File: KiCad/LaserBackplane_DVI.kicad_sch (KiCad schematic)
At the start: 45 parts, among them J1 Curr. Mod., J2 DVI-I, J3 Ld+, J4 Ld-, J5 Pz+, J6 Pz-, J7 Piezo_In, K1 G6AU, Q1 MMBT3904, Q2 2N4401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

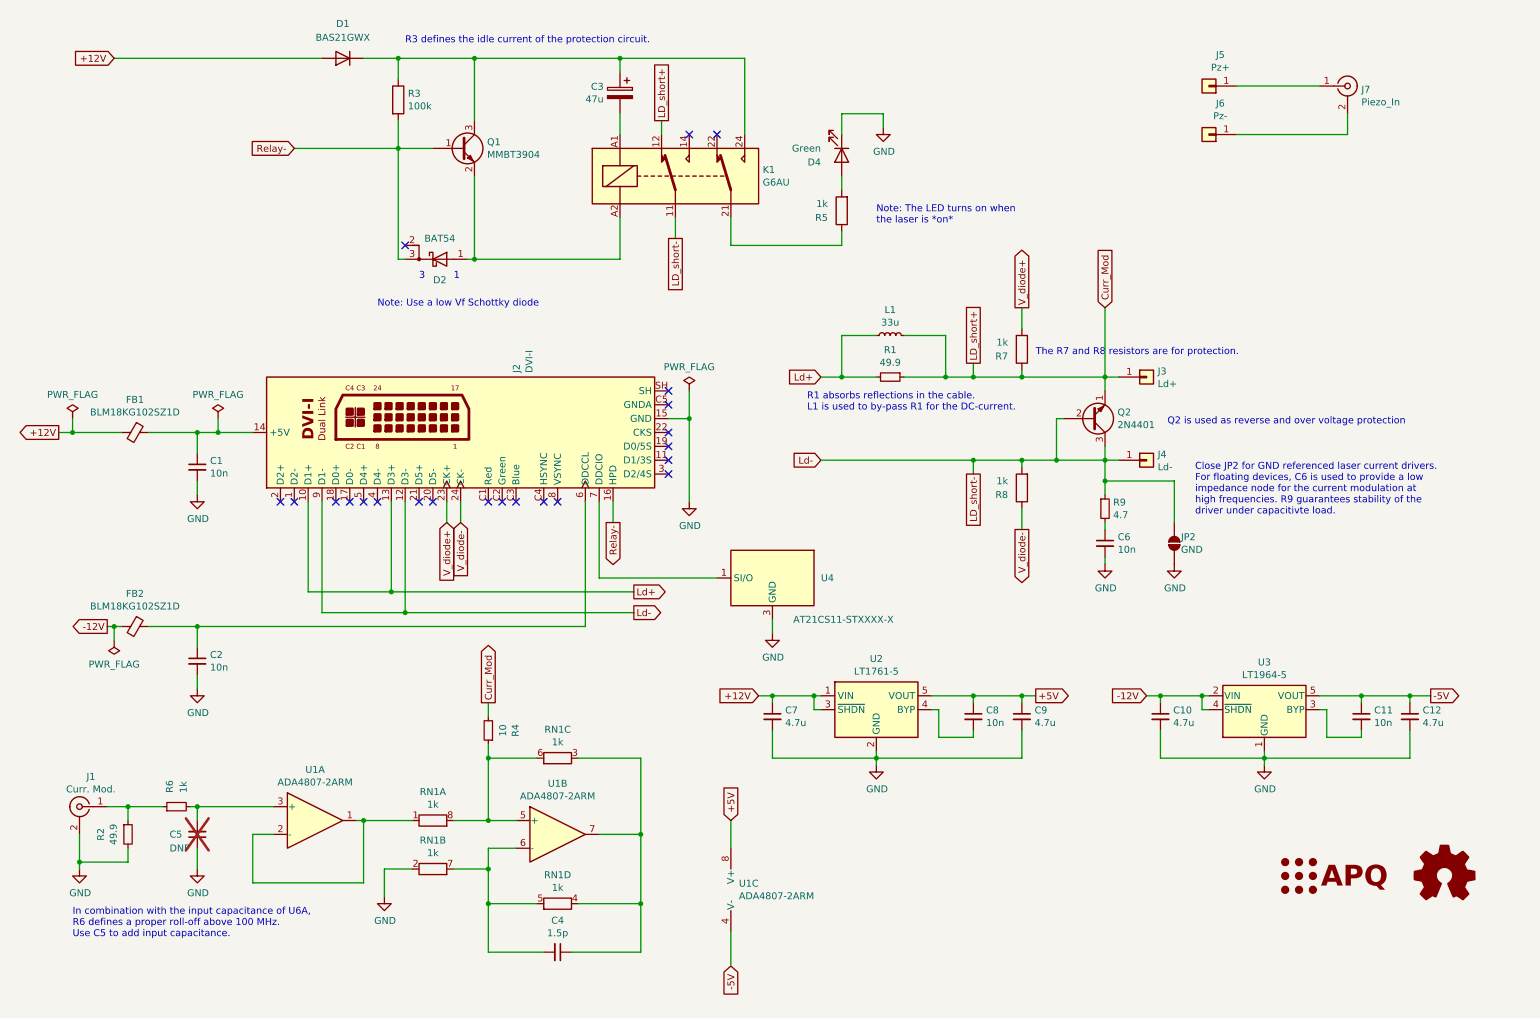
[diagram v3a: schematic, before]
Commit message: Updated parts
- Swapped 50 ohm resistor for a higher wattage part
- Added bypass capacitors to the current source opamp
- Put all parts on a 0.25 mm grid
- Improved routing
- Removed ground layer keepout below the current source, because there is no significant coupling at 1.6 mm distance
- Added RoHS information
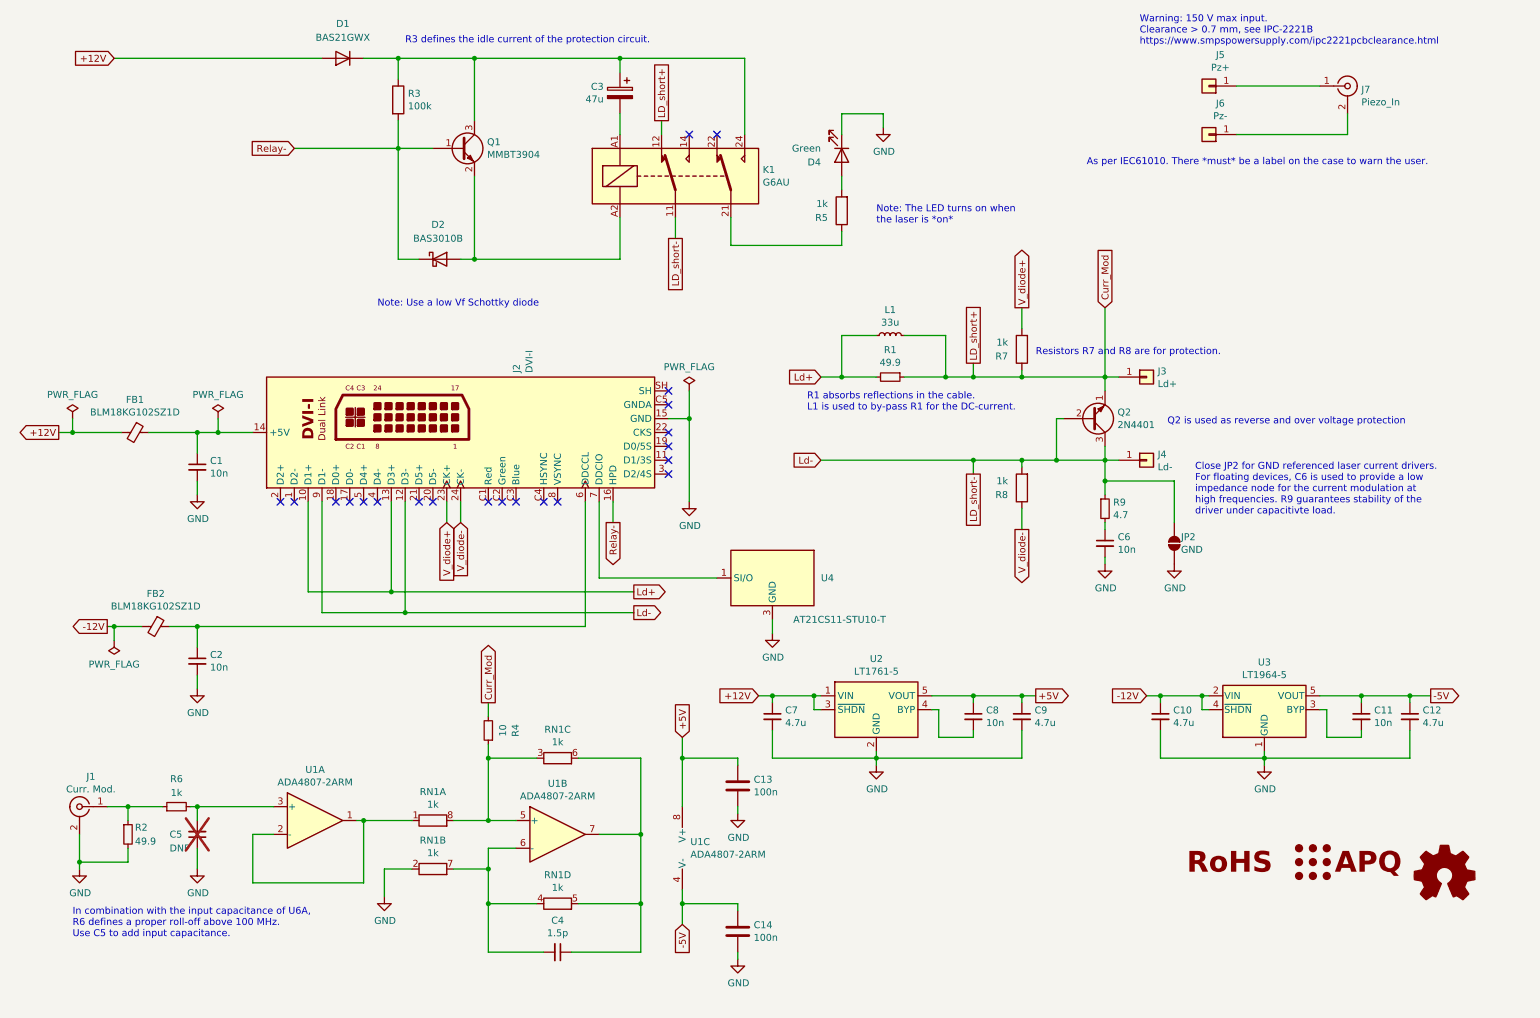
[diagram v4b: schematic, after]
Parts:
- removed D2: BAT54, Package_TO_SOT_SMD:SOT-23, symbol Device:D_Schottky_AKK
- added C13, C14: 100n, Capacitor_SMD:C_0603_1608Metric, symbol Device:C
- added D2: BAS3010B, Diode_SMD:D_SOD-323, symbol Device:D_Schottky
- added LOGO3: Logo_RoHS, Symbol:RoHS-Logo_6mm_SilkScreen, symbol Custom_logos:SYM_RoHS
- C1, C11, C2, C6, C8, FB1, FB2, RN1: RoHS (none) -> Yes; Temperature (none) -> Tstorage = –55 °C to 125 °C
- C10, C12, C7, C9: MFN Murata Electronics -> TDK; PN GRM21BR61H475KE51L -> CGA4J1X7R1V475K125AC; RoHS (none) -> Yes; Temperature (none) -> Tstorage = –55 °C to 125 °C
- C3: RoHS (none) -> Yes; Temperature (none) -> Tstorage = –40 °C to 105 °C
- C4: MFN Yageo -> Kemet; PN CC0603CPNPO9BN1R5 -> C0603C159C5GACAUTO; RoHS (none) -> Yes; Temperature (none) -> Tstorage = –55 °C to 125 °C
- D1: RoHS (none) -> Yes; Temperature (none) -> Tstorage = –65 °C to 150 °C
- D4: RoHS (none) -> Yes; Temperature (none) -> Tstorage = –40 °C to 85 °C
- J1: RoHS (none) -> By exemption; Temperature (none) -> Tstorage = –65 °C to 165 °C
- J2: MFN Conn_Link -> Conn-Link Technology Inc.; RoHS (none) -> Yes; Temperature (none) -> Tstorage = –20 °C to 85 °C
- J7: RoHS (none) -> Yes; Temperature (none) -> Tstorage = –65 °C to 165 °C
- K1: RoHS (none) -> Yes; Temperature (none) -> Tstorage = –40 °C to 70 °C
- L1: RoHS (none) -> Yes; Temperature (none) -> Tstorage = –40 °C to 165 °C
- Q1: PN MMBT3904VL -> MMBT3904-QR; RoHS (none) -> Yes; Temperature (none) -> Tstorage = –65 °C to 150 °C
- Q2: RoHS (none) -> Yes; Temperature (none) -> Tstorage = –55 °C to 150 °C
- R1: footprint Resistor_SMD:R_0603_1608Metric -> Resistor_SMD:R_0805_2012Metric; PN RR0816Q-49R9-D-68R -> RG2012P-49R9-D-T5; RoHS (none) -> Yes; Temperature (none) -> Tstorage = –55 °C to 155 °C
- R2: footprint Resistor_SMD:R_1210_3225Metric -> Resistor_SMD:R_0612_1632Metric; MFN Yageo -> ROHM Semiconductor; PN RC1210FR-0749R9L -> LTR18EZPF49R9; RoHS (none) -> By exemption; Temperature (none) -> Tstorage = –55 °C to 155 °C
- R3: RoHS (none) -> By exemption; Temperature (none) -> Tstorage = –55 °C to 155 °C
- R4: PN RR0816Q-100-D -> RG1608Q-100-D-T5; RoHS (none) -> Yes; Temperature (none) -> Tstorage = –55 °C to 155 °C
- R5, R6, R7, R8: RoHS (none) -> Yes; Temperature (none) -> Tstorage = –55 °C to 155 °C
- R9: MFN Panasonic -> SEI Stackpole; PN ERJ-3RQF4R7V -> RNCP0603FTD4R70; RoHS (none) -> Yes; Temperature (none) -> Tstorage = –55 °C to 155 °C
- U1: RoHS (none) -> Yes; Temperature (none) -> Tstorage = –40 °C to 125 °C
- U2: PN LT1761ES5-5#TRPBF -> LT1761IS5-5#TRPBF; RoHS (none) -> Yes; Temperature (none) -> Tstorage = –40 °C to 125 °C
- U3: PN LT1964ES5-5#TRPBF -> LT1964IS5-5#TRPBF; RoHS (none) -> Yes; Temperature (none) -> Tstorage = –40 °C to 125 °C
- U4: value AT21CS11-STXXXX-X -> AT21CS11-STU10-T; MFN (none) -> Microchip Technology; PN (none) -> AT21CS11-STU10-T; RoHS (none) -> Yes; Temperature (none) -> Tstorage = –40 °C to 85 °C
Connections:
- net +5V: now also C13.1
- net -5V: now also C14.1
- net GND: now also C13.2, C14.2
- net Relay-: now also D2.1 (K)
- net at K1.A2, Q1.2 (E): now also D2.2 (A)
- net at R4.1, RN1.8 (R1.2), U1.5 (+): now also RN1.3 (R3.1); no longer RN1.6 (R3.2)
- net at C4.2, RN1.7 (R2.2), U1.6 (-): now also RN1.4 (R4.1); no longer RN1.5 (R4.2)
- net at C4.1, U1.7: now also RN1.5 (R4.2), RN1.6 (R3.2); no longer RN1.3 (R3.1), RN1.4 (R4.1)
- no-connect marks 22 -> 21
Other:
- note added: "As per IEC61010. There *must* be a label on the case to warn the user."
- note added: "Resistors R7 and R8 are for protection."
- note added: "Warning: 150 V max input. Clearance > 0.7 mm, see IPC-2221B https://www.smpspowersupply.com/ipc2221pcbclearance.html"
- note removed: "1"
- note removed: "3"
- note removed: "The R7 and R8 resistors are for protection."
- moved on the sheet: FB2, RN1C, RN1D, U1C

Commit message: Place bypass capacitors only when using the current mod variant
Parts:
- C13, C14: Config (none) -> +curr_mod; variant (none) -> curr_mod
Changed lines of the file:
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@@
+			)
+		)
+		(property "Config" "+curr_mod"
+			(at 146.05 184.15 0)
+			(effects
+				(font
+					(size 1.27 1.27)
+				)
+				(hide yes)
+			)
+		)
+		(property "variant" "curr_mod"
+			(at 146.05 184.15 0)
+			(effects
+				(font
+					(size 1.27 1.27)
+				)
+				(hide yes)
 			)
 		)
@@
 				)
 				(hide yes)
+			)
+		)
+		(property "Config" "+curr_mod"
+			(at 146.05 157.48 0)
+			(effects
+				(font
+					(size 1.27 1.27)
+				)
+				(hide yes)
+			)
+		)
+		(property "variant" "curr_mod"
+			(at 146.05 157.48 0)
+			(effects
+				(font
+					(size 1.27 1.27)
+				)
+				(hide yes)

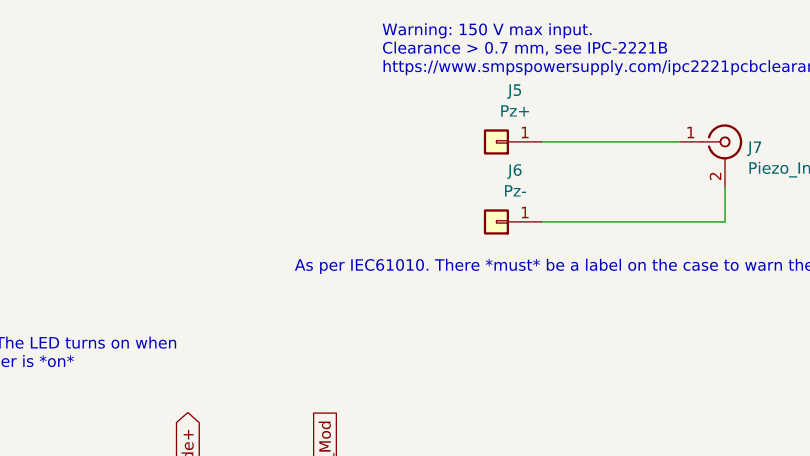
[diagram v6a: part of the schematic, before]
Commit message: 1.7.4 (#5)
* Add chamfer to corners

* Change line with of the part dimentsions to 0.1 mm

* Add teardrops

* Added peizo driver high voltage warning

* Add PCBA variant

* Cleaned up labels

* Create individual gerber files for all variants to make sure DNP parts are not included in the mask layer
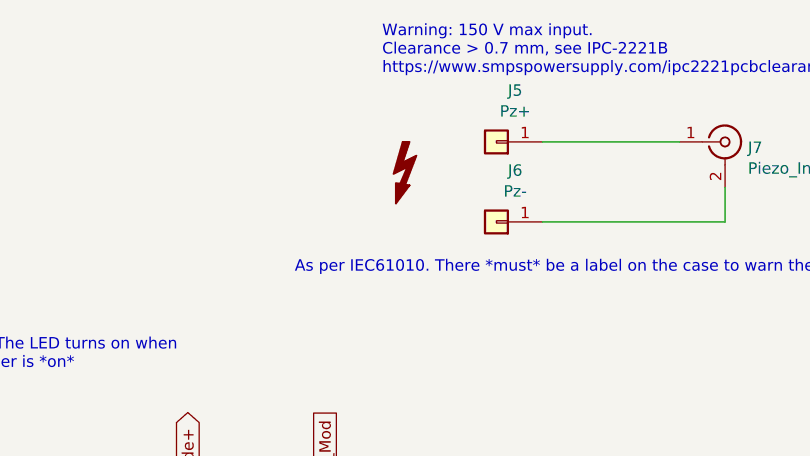
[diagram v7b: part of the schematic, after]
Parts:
- added SYM1: SYM_Flash_Small, custom:Symbol_HighVoltage_Triangle_3x3mm, symbol Graphic:SYM_Flash_Small
- J2: Config (none) -> -PCBA
- R4: PN RG1608Q-100-D-T5 -> RG1608Q-100-D-T5
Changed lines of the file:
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@@
 			)
 		)
+		(property "Config" "-PCBA"
+			(at 95.25 92.71 0)
+			(effects
+				(font
+					(size 1.27 1.27)
+				)
+				(hide yes)
+			)
+		)
 		(property "RoHS" "Yes"
 			(at 95.25 92.71 0)
@@
 			)
 		)
-		(property "Description" "Monostable Relay DPDT, EN50005 "
+		(property "Description" "Monostable Relay DPDT, EN50005"
 			(at 134.62 45.72 0)
 			(effects
@@
 			)
 		)
-		(property "PN" "RG1608Q-100-D-T5 "
+		(property "PN" "RG1608Q-100-D-T5"
 			(at 100.33 147.32 90)
 			(effects
@@
 					(unit 1)
 				)
+			)
+		)
+	)
+	(symbol
+		(lib_id "Graphic:SYM_Flash_Small")
+		(at 222.25 33.02 0)
+		(unit 1)
+		(exclude_from_sim yes)
+		(in_bom no)
+		(on_board yes)
+		(dnp no)
+		(fields_autoplaced yes)
+		(property "Reference" "SYM1"
+			(at 219.964 33.02 90)
+			(effects
+				(font
+					(size 1.27 1.27)
+				)
+				(hide yes)
+			)
+		)
+		(property "Value" "SYM_Flash_Small"
+			(at 224.536 33.02 90)
+			(effects
+				(font
+					(size 1.27 1.27)
+				)
+				(hide yes)
+			)
+		)
+		(property "Footprint" "custom:Symbol_HighVoltage_Triangle_3x3mm"
+			(at 222.25 33.655 0)
+			(effects
+				(font
+					(size 1.27 1.27)
+				)
+				(hide yes)
+			)
+		)
+		(property "Datasheet" "~"
+			(at 232.41 35.56 0)
+			(effects
+				(font
+					(size 1.27 1.27)
+				)
+				(hide yes)
+			)
+		)
+		(property "Description" "Flash symbol, small"
+			(at 222.25 33.02 0)
+			(effects
+				(font
+					(size 1.27 1.27)
+				)
+				(hide yes)
+			)
+		)
+		(property "MFN" ""
+			(at 222.25 33.02 0)
+			(effects
+				(font
+					(size 1.27 1.27)
+				)
+				(hide yes)
+			)
+		)
+		(property "PN" ""
+			(at 222.25 33.02 0)
+			(effects
+				(font
+					(size 1.27 1.27)
+				)
+				(hide yes)
+			)
+		)
+		(instances
+			(project "LaserBackplane_DVI"
+				(path "/cb6062da-8dcd-4826-92fd-4071e9e97213"
+					(reference "SYM1")
+					(unit 1)
+				)

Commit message: Replaced 10nF X7R CGA3E2X7R1H103K080AA with C0G CGA3E2C0G1H103J080AE
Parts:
- C1, C11, C6, C8: PN CGA3E2X7R1H103K080AA -> CGA3E2C0G1H103J080AE
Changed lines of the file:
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@@
 			)
 		)
-		(property "PN" "CGA3E2X7R1H103K080AA"
+		(property "PN" "CGA3E2C0G1H103J080AE"
 			(at 46.99 99.06 0)
 			(effects
@@
 			)
 		)
-		(property "PN" "CGA3E2X7R1H103K080AA"
+		(property "PN" "CGA3E2C0G1H103J080AE"
 			(at 189.23 144.78 0)
 			(effects
@@
 			)
 		)
-		(property "PN" "CGA3E2X7R1H103K080AA"
+		(property "PN" "CGA3E2C0G1H103J080AE"
 			(at 260.35 144.78 0)
 			(effects
@@
 			)
 		)
-		(property "PN" "CGA3E2X7R1H103K080AA"
+		(property "PN" "CGA3E2C0G1H103J080AE"
 			(at 213.36 113.03 0)
 			(effects
